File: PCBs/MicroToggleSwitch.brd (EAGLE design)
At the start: 14.5 x 42 mm, 3 parts

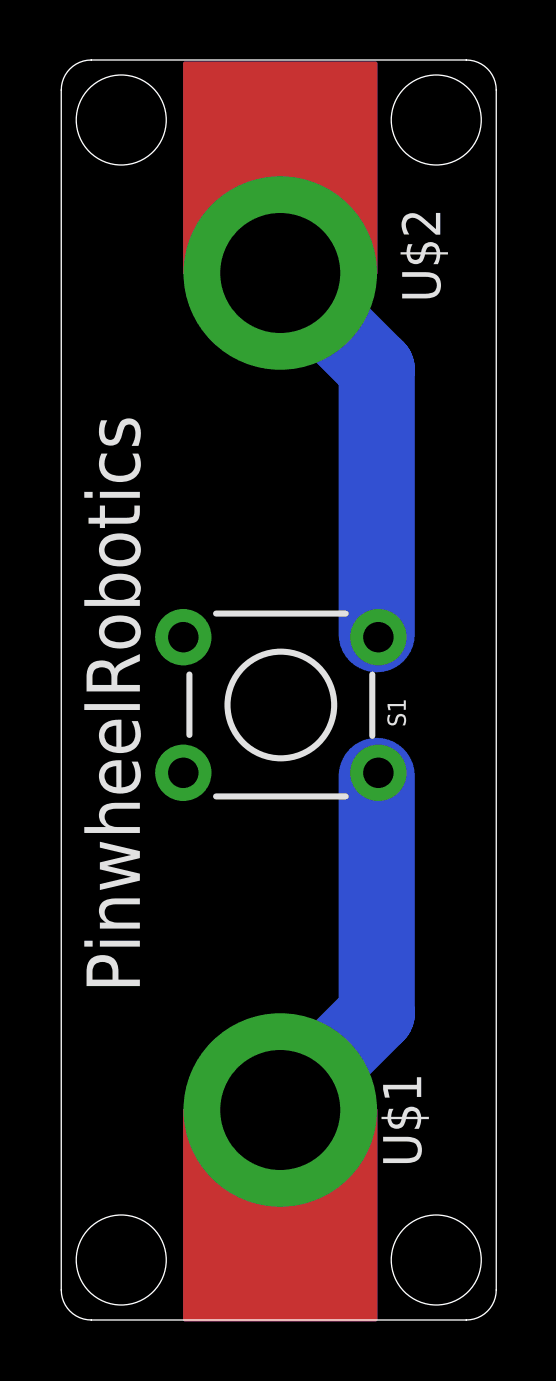
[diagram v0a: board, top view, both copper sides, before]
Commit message: Update for Dim width is 42 length is 28 for type 2 pcb
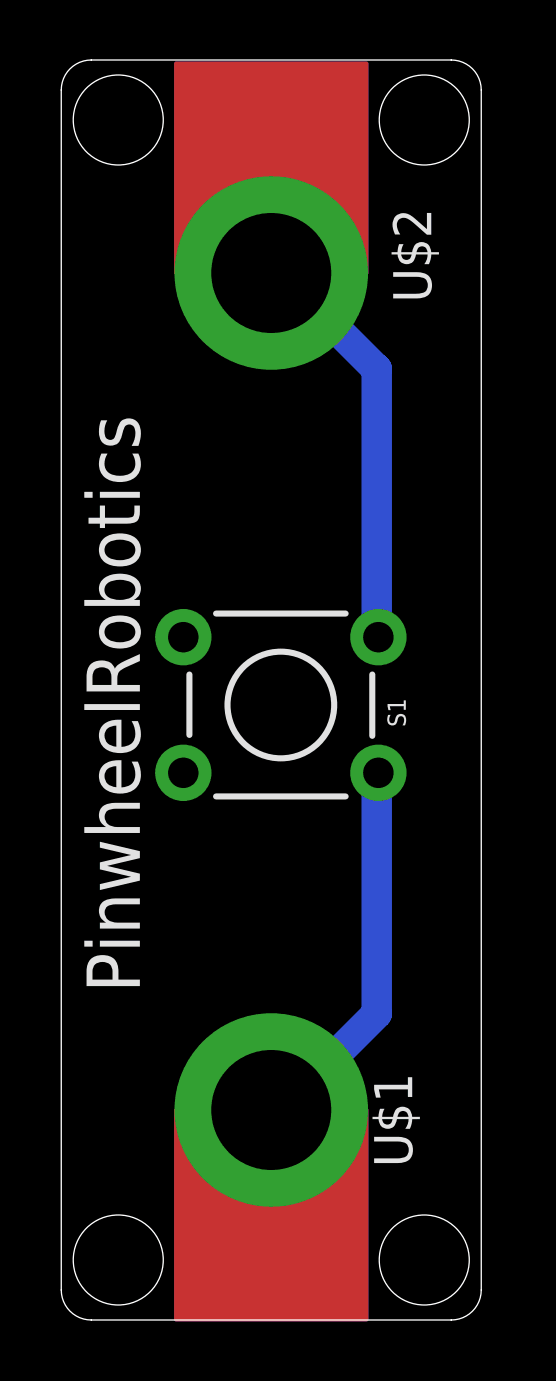
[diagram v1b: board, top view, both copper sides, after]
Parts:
- moved U$1 0.30 mm to (7.00, 7.00)
- moved U$2 0.30 mm to (7.00, 34.9)
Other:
- board size 14.5 x 42 mm -> 14 x 42 mm
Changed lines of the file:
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@@
 <drawing>
 <settings>
-<setting alwaysvectorfont="no"/>
+<setting alwaysvectorfont="yes"/>
 <setting verticaltext="up"/>
 </settings>
@@
 <board>
 <plain>
+<wire x1="13" y1="42" x2="1" y2="42" width="0" layer="20"/>
+<wire x1="1" y1="42" x2="0" y2="41" width="0" layer="20" curve="90"/>
 <wire x1="0" y1="41" x2="0" y2="1" width="0" layer="20"/>
 <wire x1="0" y1="1" x2="1" y2="0" width="0" layer="20" curve="90"/>
-<wire x1="1" y1="0" x2="13.5" y2="0" width="0" layer="20"/>
-<wire x1="13.5" y1="0" x2="14.5" y2="1" width="0" layer="20" curve="90"/>
-<wire x1="14.5" y1="1" x2="14.5" y2="41" width="0" layer="20"/>
-<wire x1="14.5" y1="41" x2="13.5" y2="42" width="0" layer="20" curve="90"/>
-<wire x1="13.5" y1="42" x2="1" y2="42" width="0" layer="20"/>
-<wire x1="1" y1="42" x2="0" y2="41" width="0" layer="20" curve="90"/>
-<hole x="2" y="40" drill="3"/>
-<hole x="12.5" y="40" drill="3"/>
-<hole x="2" y="2" drill="3"/>
-<hole x="12.5" y="2" drill="3"/>
+<wire x1="1" y1="0" x2="13" y2="0" width="0" layer="20"/>
+<wire x1="13" y1="0" x2="14" y2="1" width="0" layer="20" curve="90"/>
+<wire x1="14" y1="1" x2="14" y2="41" width="0" layer="20"/>
+<wire x1="14" y1="41" x2="13" y2="42" width="0" layer="20" curve="90"/>
+<hole x="1.9" y="40" drill="3"/>
+<hole x="12.1" y="40" drill="3"/>
+<hole x="1.9" y="2" drill="3"/>
+<hole x="12.1" y="2" drill="3"/>
 <text x="2.621" y="10.915" size="1.778" layer="21" rot="R90">PinwheelRobotics </text>
 <text x="13.551" y="29.457" size="1.778" layer="22" rot="MR270">care@pinwheel.in</text>
 <dimension x1="-1.5" y1="42" x2="-1.5" y2="0" x3="-12.5" y3="21" textsize="1.778" layer="1"/>
 <dimension x1="0" y1="42.5" x2="14.5" y2="42.5" x3="7.25" y3="49.5" textsize="1.778" layer="1"/>
+<dimension x1="0" y1="45" x2="14" y2="45" x3="7" y3="44" textsize="1.778" layer="1"/>
+<dimension x1="16" y1="2" x2="16" y2="40" x3="14.5" y3="21" textsize="1.778" layer="1"/>
 </plain>
 <attributes>
@@
 <attribute name="SF_SKU" value="COM-00097" x="-14.27" y="56.06" size="1.778" layer="27" rot="R180" display="off"/>
 </element>
-<element name="U$1" library="microbit" package="MICROBIT_PAD" value="MICROBIT_PAD" x="7.3" y="7" smashed="yes">
-<attribute name="NAME" x="11.999" y="5.095" size="1.27" layer="21" rot="R90"/>
+<element name="U$1" library="microbit" package="MICROBIT_PAD" value="MICROBIT_PAD" x="7" y="7" smashed="yes">
+<attribute name="NAME" x="11.699" y="5.095" size="1.27" layer="21" rot="R90"/>
 </element>
-<element name="U$2" library="microbit" package="MICROBIT_PAD" value="MICROBIT_PAD" x="7.3" y="34.9" smashed="yes" rot="R180">
-<attribute name="NAME" x="11.364" y="37.059" size="1.27" layer="21" rot="R270"/>
+<element name="U$2" library="microbit" package="MICROBIT_PAD" value="MICROBIT_PAD" x="7" y="34.9" smashed="yes" rot="R180">
+<attribute name="NAME" x="11.064" y="37.059" size="1.27" layer="21" rot="R270"/>
 </element>
 </elements>
@@
 <contactref element="U$1" pad="PAD"/>
 <contactref element="S1" pad="1"/>
-<wire x1="10.5156" y1="10.2108" x2="10.5156" y2="18.1356" width="2.54" layer="16"/>
-<wire x1="7.3152" y1="7.0104" x2="10.5156" y2="10.2108" width="2.54" layer="16"/>
+<wire x1="10.5156" y1="10.2108" x2="10.5156" y2="18.1356" width="1.016" layer="16"/>
+<wire x1="7.3152" y1="7.0104" x2="10.5156" y2="10.2108" width="1.016" layer="16"/>
 <wire x1="10.5156" y1="18.1356" x2="10.5712" y2="18.2394" width="0.1524" layer="16"/>
-<wire x1="7.3152" y1="7.0104" x2="7.3" y2="7" width="0.1524" layer="16"/>
+<wire x1="7.3152" y1="7.0104" x2="7" y2="7" width="0.1524" layer="16"/>
 </signal>
 <signal name="N$2">
 <contactref element="U$2" pad="PAD"/>
 <contactref element="S1" pad="3"/>
-<wire x1="10.5156" y1="31.6992" x2="10.5156" y2="22.86" width="2.54" layer="16"/>
-<wire x1="7.3152" y1="34.8996" x2="10.5156" y2="31.6992" width="2.54" layer="16"/>
+<wire x1="10.5156" y1="31.6992" x2="10.5156" y2="22.86" width="1.016" layer="16"/>
+<wire x1="7.3152" y1="34.8996" x2="10.5156" y2="31.6992" width="1.016" layer="16"/>
 <wire x1="10.5156" y1="22.86" x2="10.5712" y2="22.7606" width="0.1524" layer="16"/>
-<wire x1="7.3152" y1="34.8996" x2="7.3" y2="34.9" width="0.1524" layer="16"/>
+<wire x1="7.3152" y1="34.8996" x2="7" y2="34.9" width="0.1524" layer="16"/>
 </signal>
 </signals>

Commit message: Corrected hole position for some design , made transistor as switch as category 1
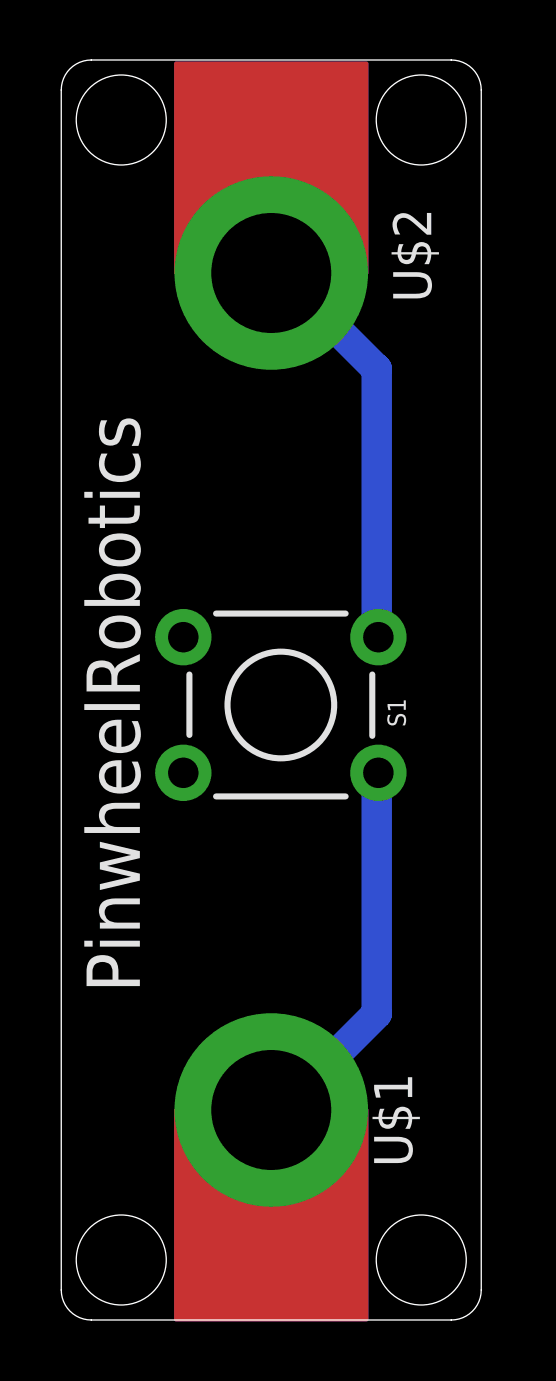
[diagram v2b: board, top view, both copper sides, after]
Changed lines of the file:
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@@
 <drawing>
 <settings>
-<setting alwaysvectorfont="yes"/>
+<setting alwaysvectorfont="no"/>
 <setting verticaltext="up"/>
 </settings>
@@
 <wire x1="14" y1="1" x2="14" y2="41" width="0" layer="20"/>
 <wire x1="14" y1="41" x2="13" y2="42" width="0" layer="20" curve="90"/>
-<hole x="1.9" y="40" drill="3"/>
-<hole x="12.1" y="40" drill="3"/>
-<hole x="1.9" y="2" drill="3"/>
-<hole x="12.1" y="2" drill="3"/>
+<hole x="2" y="40" drill="3"/>
+<hole x="12" y="40" drill="3"/>
+<hole x="2" y="2" drill="3"/>
+<hole x="12" y="2" drill="3"/>
 <text x="2.621" y="10.915" size="1.778" layer="21" rot="R90">PinwheelRobotics </text>
 <text x="13.551" y="29.457" size="1.778" layer="22" rot="MR270">care@pinwheel.in</text>
